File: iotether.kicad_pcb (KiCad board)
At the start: 2 copper layers, 100 x 100 mm, 183 parts, among them J101 USB_B_Micro, J102 Barrel_Jack, J103 Conn_02x04_Odd_Even, J201 Conn_02x04_Top_Bottom, J202 8P8C_LED_Shielded, J203 Conn_01x04, J204 Conn_01x08, J205 Conn_01x04, J206 Conn_01x04, J207 Conn_01x04, J208 Conn_01x04, J301 Conn_01x12, J302 Conn_01x12, J303 Conn_01x12, J304 Conn_01x12, J401 Conn_01x04, J402 Conn_02x04_Odd_Even, J403 Barrel_Jack_Switch, J404 Conn_01x02, J405 Conn_01x02, J406 Conn_01x02, J407 Conn_01x02, J408 Conn_01x04, J409 Conn_01x06, K401 G5LE-1, Q401 DMG3414U, Q402 AO3401A, Q403 AO3401A, Q404 AO3401A, U101 LAN9514, U102 93CxxC, U103 LM1117-3.3, U104 MCP73831-2-OT, U201 SN74CBT3253, U202 PCF8574, U301 FT4232H, U302 93CxxC, U401 MCP2221AxSL, U402 MAX232, U403 PCF8574, U404 PC817, U405 PC817, U406 PC817, U407 PC817, U408 LM75B, U409 DS1307+, Y101 Crystal, Y301 Crystal, Y401 Crystal

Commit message: Add IoTether 2, fix the USB on IoTether 1
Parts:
- J101: footprint Connector_USB:USB_Micro-B_Wuerth_629105150521 -> Connector_PinHeader_2.54mm:PinHeader_1x06_P2.54mm_Vertical
- moved J101 8.54 mm to (77.9, 86.0), turned to 0 degrees
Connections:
- J101 pad 4: Net-(J101-Pad4) -> unconnected-(J101-Pad4)
- J202 pad 4: Net-(J202-Pad4) -> unconnected-(J202-Pad4)
- J202 pad 5: Net-(J202-Pad5) -> unconnected-(J202-Pad5)
- J202 pad 6: Net-(J202-Pad6) -> unconnected-(J202-Pad6)
- J403 pad 3: Net-(J403-Pad3) -> unconnected-(J403-Pad3)
- JP102 pad 2: Net-(JP102-Pad2) -> unconnected-(JP102-Pad2)
- JP103 pad 2: Net-(JP103-Pad2) -> unconnected-(JP103-Pad2)
- JP201 pad 1: Net-(JP201-Pad1) -> unconnected-(JP201-Pad1)
- JP202 pad 1: Net-(JP202-Pad1) -> unconnected-(JP202-Pad1)
- JP203 pad 1: Net-(JP203-Pad1) -> unconnected-(JP203-Pad1)
- JP204 pad 1: Net-(JP204-Pad1) -> unconnected-(JP204-Pad1)
- K401 pad 4: Net-(K401-Pad4) -> unconnected-(K401-Pad4)
- U101 pad 13: Net-(U101-Pad13) -> unconnected-(U101-Pad13)
- U101 pad 31: Net-(U101-Pad31) -> unconnected-(U101-Pad31)
- U101 pad 35: Net-(U101-Pad35) -> unconnected-(U101-Pad35)
- U101 pad 36: Net-(U101-Pad36) -> unconnected-(U101-Pad36)
- U101 pad 37: Net-(U101-Pad37) -> unconnected-(U101-Pad37)
- U101 pad 42: Net-(U101-Pad42) -> unconnected-(U101-Pad42)
- U101 pad 43: Net-(U101-Pad43) -> unconnected-(U101-Pad43)
- U101 pad 45: Net-(U101-Pad45) -> unconnected-(U101-Pad45)
- U101 pad 47: Net-(U101-Pad47) -> unconnected-(U101-Pad47)
- U102 pad 7: Net-(U102-Pad7) -> unconnected-(U102-Pad7)
- U202 pad 13: Net-(U202-Pad13) -> unconnected-(U202-Pad13)
- U301 pad 36: Net-(U301-Pad36) -> unconnected-(U301-Pad36)
- U301 pad 60: Net-(U301-Pad60) -> unconnected-(U301-Pad60)
- U302 pad 7: Net-(U302-Pad7) -> unconnected-(U302-Pad7)
- U401 pad 4: Net-(U401-Pad4) -> unconnected-(U401-Pad4)
- U402 pad 10: Net-(U402-Pad10) -> unconnected-(U402-Pad10)
- U402 pad 7: Net-(U402-Pad7) -> unconnected-(U402-Pad7)
- U402 pad 8: Net-(U402-Pad8) -> unconnected-(U402-Pad8)
- U402 pad 9: Net-(U402-Pad9) -> unconnected-(U402-Pad9)
- U403 pad 13: Net-(U403-Pad13) -> unconnected-(U403-Pad13)
- U408 pad 3: Net-(U408-Pad3) -> unconnected-(U408-Pad3)
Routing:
- net UP_D+: track 32.4 -> 38.5 mm
- net +5V: track 581.3 -> 576.0 mm, vias 17 -> 16
- net UP_D-: track 32.6 -> 37.4 mm
- net GND: track 214.9 -> 212.4 mm
- net VBUS: track 73.2 -> 73.9 mm
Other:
- net class Default removed

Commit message: Add i2c_sampler, update to revision 3
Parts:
- removed C401: 1uF, Capacitor_SMD:C_0805_2012Metric_Pad1.18x1.45mm_HandSolder
- removed C402, C403, C404, C405: 1uF, Capacitor_SMD:C_0805_2012Metric_Pad1.15x1.40mm_HandSolder
- removed D401, D403, D404, D405: LED, LED_SMD:LED_0603_1608Metric_Pad1.05x0.95mm_HandSolder
- removed D402: D, Diode_THT:D_DO-35_SOD27_P2.54mm_Vertical_AnodeUp
- removed J203, J408: Conn_01x04, Connector_PinHeader_2.54mm:PinHeader_1x04_P2.54mm_Vertical
- removed J204: Conn_01x08, Connector_PinHeader_2.54mm:PinHeader_2x04_P2.54mm_Vertical
- removed J401: Conn_01x04, Connector_PinHeader_2.54mm:PinHeader_1x04_P2.54mm_Horizontal
- removed J402: Conn_02x04_Odd_Even, Connector_PinHeader_2.54mm:PinHeader_2x04_P2.54mm_Vertical
- removed J403: Barrel_Jack_Switch, Connector_BarrelJack:BarrelJack_Horizontal
- removed J404, J405, J406, J407: Conn_01x02, TerminalBlock:TerminalBlock_bornier-2_P5.08mm
- removed J409: Conn_01x06, Connector_PinHeader_2.54mm:PinHeader_1x06_P2.54mm_Horizontal
- removed JP401, JP402, JP403: Jumper, Resistor_SMD:R_1206_3216Metric
- removed K401: G5LE-1, Relay_THT:Relay_SPDT_Omron-G5LE-1
- removed Q401: DMG3414U, Package_TO_SOT_SMD:SOT-23
- removed Q402, Q403, Q404: AO3401A, Package_TO_SOT_SMD:SOT-23
- removed R401: 47k, Resistor_SMD:R_0603_1608Metric_Pad1.05x0.95mm_HandSolder
- removed R402, R403: 2.2k, Resistor_SMD:R_0603_1608Metric_Pad1.05x0.95mm_HandSolder
- removed R404, R413, R414, R415: 470, Resistor_SMD:R_0603_1608Metric_Pad1.05x0.95mm_HandSolder
- removed R405, R410, R411, R412: 1k, Resistor_SMD:R_0603_1608Metric_Pad1.05x0.95mm_HandSolder
- removed R406, R407, R408, R409: 100k, Resistor_SMD:R_0603_1608Metric_Pad1.05x0.95mm_HandSolder
- removed RN401: 220, Resistor_THT:R_Array_SIP5
- removed U202, U403: PCF8574, Package_SO:SOIC-16W_7.5x10.3mm_P1.27mm
- removed U401: MCP2221AxSL, Package_SO:SOIC-14_3.9x8.7mm_P1.27mm
- removed U402: MAX232, Package_DIP:DIP-16_W7.62mm_Socket
- removed U404, U405, U406, U407: PC817, Package_DIP:DIP-4_W7.62mm
- added C126: C, Capacitor_SMD:C_0603_1608Metric, B.Cu at (90.9, 97.0)
- added C127: C, Capacitor_THT:CP_Radial_D8.0mm_P3.80mm, F.Cu at (86.3, 93.5)
- added C309: 22pf, Capacitor_SMD:C_0805_2012Metric_Pad1.18x1.45mm_HandSolder, B.Cu at (152.5, 91.5)
- added C310: 22pf, Capacitor_SMD:C_0805_2012Metric_Pad1.18x1.45mm_HandSolder, B.Cu at (152.5, 93.6)
- added C311: C, Capacitor_SMD:C_0603_1608Metric_Pad1.08x0.95mm_HandSolder, F.Cu at (145.1, 138.0)
- added C312: .1uf, Capacitor_SMD:C_0603_1608Metric_Pad1.08x0.95mm_HandSolder, B.Cu at (136.4, 71.3)
- added C313: C, Capacitor_SMD:C_0805_2012Metric_Pad1.18x1.45mm_HandSolder, B.Cu at (140.2, 73.3)
- added C314: C, Capacitor_SMD:C_0805_2012Metric_Pad1.18x1.45mm_HandSolder, B.Cu at (140.2, 70.0)
- added C315: C, Capacitor_SMD:C_0805_2012Metric_Pad1.18x1.45mm_HandSolder, B.Cu at (149.1, 74.5)
- added C316: C, Capacitor_SMD:C_0805_2012Metric_Pad1.18x1.45mm_HandSolder, B.Cu at (147.0, 74.5)
- added D203: LED, LED_SMD:LED_0603_1608Metric_Pad1.05x0.95mm_HandSolder, F.Cu at (125.2, 98.6)
- added J305: Conn_02x04_Odd_Even, Connector_PinHeader_2.54mm:PinHeader_2x04_P2.54mm_Vertical, F.Cu at (122.0, 115.3)
- added J306: Conn_01x09, Connector_USB:USB_A_Wuerth_61400826021_Horizontal_Stacked, F.Cu at (142.9, 59.0)
- added J307: Conn_01x09, Connector_USB:USB_A_Wuerth_61400826021_Horizontal_Stacked, F.Cu at (161.1, 59.0)
- added L102: L, Inductor_SMD:L_1210_3225Metric_Pad1.42x2.65mm_HandSolder, B.Cu at (96.0, 101.6)
- added R107: R, Resistor_SMD:R_0805_2012Metric, B.Cu at (107.7, 98.0)
- added R108: R, Resistor_SMD:R_0603_1608Metric, F.Cu at (92.0, 99.6)
- added R109: R, Resistor_SMD:R_0603_1608Metric, F.Cu at (92.0, 97.9)
- added R224: 470, Resistor_SMD:R_0603_1608Metric_Pad0.98x0.95mm_HandSolder, B.Cu at (128.3, 101.0)
- added R307: R, Resistor_SMD:R_0603_1608Metric_Pad0.98x0.95mm_HandSolder, F.Cu at (147.6, 111.6)
- added R308: R, Resistor_SMD:R_0603_1608Metric_Pad0.98x0.95mm_HandSolder, F.Cu at (147.6, 106.9)
- added R309: R, Resistor_SMD:R_0603_1608Metric_Pad0.98x0.95mm_HandSolder, B.Cu at (112.6, 140.0)
- added R310: R, Resistor_SMD:R_0603_1608Metric_Pad0.98x0.95mm_HandSolder, F.Cu at (149.2, 106.9)
- added R311: R, Resistor_SMD:R_0603_1608Metric_Pad0.98x0.95mm_HandSolder, B.Cu at (113.5, 141.7)
- added R312: 2.2k, Resistor_SMD:R_0603_1608Metric_Pad0.98x0.95mm_HandSolder, B.Cu at (140.9, 111.2)
- added R313: 2.2k, Resistor_SMD:R_0603_1608Metric_Pad0.98x0.95mm_HandSolder, B.Cu at (140.9, 112.8)
- added R314: R, Resistor_SMD:R_0603_1608Metric_Pad0.98x0.95mm_HandSolder, B.Cu at (153.9, 84.9)
- added R315: R, Resistor_SMD:R_0603_1608Metric_Pad0.98x0.95mm_HandSolder, F.Cu at (149.2, 85.6)
- added R316: R, Resistor_SMD:R_0603_1608Metric_Pad0.98x0.95mm_HandSolder, F.Cu at (149.2, 84.0)
- added R317: 15k, Resistor_SMD:R_0603_1608Metric_Pad0.98x0.95mm_HandSolder, B.Cu at (137.4, 67.5)
- added R318: R, Resistor_SMD:R_0603_1608Metric_Pad0.98x0.95mm_HandSolder, B.Cu at (135.7, 65.7)
- added R319: R, Resistor_SMD:R_0603_1608Metric_Pad0.98x0.95mm_HandSolder, B.Cu at (136.2, 60.8)
- added SW301: SW_Push, Button_Switch_THT:SW_PUSH_6mm, F.Cu at (155.8, 116.8)
- added SW302: SW_Push, Button_Switch_THT:SW_PUSH_6mm, F.Cu at (158.8, 96.5)
- added SW303: SW_Push, Button_Switch_THT:SW_PUSH_6mm, F.Cu at (158.8, 82.0)
- added SW304: SW_Push, Button_Switch_THT:SW_PUSH_6mm, F.Cu at (158.8, 72.3)
- added U105: AP62200, Package_TO_SOT_SMD:SOT-23-6, B.Cu at (91.8, 99.7)
- added U303: ATmega328P-P, Package_DIP:DIP-28_W7.62mm, F.Cu at (145.4, 112.8)
- added U304: FE1.1s, Package_SO:SSOP-28_3.9x9.9mm_P0.635mm, F.Cu at (139.4, 64.9)
- added Y302: Crystal, Crystal:Crystal_HC49-U_Vertical, F.Cu at (149.7, 90.0)
- added Y303: Crystal, Crystal:Crystal_HC49-U_Vertical, F.Cu at (149.1, 71.5)
- C102, R101, U409: moved to B.Cu
- C406: footprint Capacitor_SMD:C_0603_1608Metric_Pad1.05x0.95mm_HandSolder -> Capacitor_SMD:C_0603_1608Metric_Pad1.08x0.95mm_HandSolder; moved to F.Cu
- C407: footprint Capacitor_SMD:C_0603_1608Metric_Pad1.05x0.95mm_HandSolder -> Capacitor_SMD:C_0603_1608Metric_Pad1.08x0.95mm_HandSolder
- R106, R210, R211: footprint Resistor_SMD:R_0603_1608Metric_Pad1.05x0.95mm_HandSolder -> Resistor_SMD:R_0603_1608Metric_Pad0.98x0.95mm_HandSolder
- R416: footprint Resistor_SMD:R_0603_1608Metric_Pad1.05x0.95mm_HandSolder -> Resistor_SMD:R_0603_1608Metric_Pad0.98x0.95mm_HandSolder; moved to F.Cu
- moved H105 95.1 mm to (110.7, 135.7)
- moved J103 71.8 mm to (93.1, 79.4), turned to 0 degrees
- moved D406 66.6 mm to (108.5, 115.8), turned to 180 degrees
- moved C406 57.9 mm to (120.7, 118.3), turned to 0 degrees
- moved BT401 56.3 mm to (114.6, 119.4), turned to 90 degrees
- moved R416 55.1 mm to (112.1, 115.8), turned to 0 degrees
- moved Y401 53.8 mm to (118.5, 116.7)
- moved C407 52.9 mm to (118.5, 113.1)
- moved U408 52.1 mm to (107.1, 113.6)
- moved U409 46.2 mm to (112.8, 113.6), turned to 90 degrees
- moved H102 39.9 mm to (163.4, 92.6)
- moved R106 29.9 mm to (141.5, 54.4)
- moved C121 25.6 mm to (159.6, 65.7), turned to 0 degrees
- moved C124 24.8 mm to (129.5, 64.3), turned to -90 degrees
- moved C123 14.1 mm to (143.5, 119.9), turned to 0 degrees
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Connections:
- net /USBHub/SW0 renamed SW0
- net /USBHub/SW1 renamed SW1
- net Net-(J302-Pad3) renamed ATM_RX
- net Net-(J302-Pad4) renamed ATM_TX
- net Net-(J302-Pad7) renamed ATM_DTR
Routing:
- net Net-(R310-Pad2): track 0.00 -> 72.7 mm, vias 0 -> 2
- net Net-(R308-Pad2): track 0.00 -> 72.5 mm, vias 0 -> 2
- net ATM_DTR: track 25.3 -> 67.3 mm, vias 0 -> 1
- net Net-(J409-Pad5): track 40.9 -> 0.00 mm, vias 1 -> 0
- net /MCP2221A/ATM_RESET: track 0.00 -> 38.9 mm, vias 0 -> 3
- net Net-(D402-Pad2): track 33.7 -> 0.00 mm, vias 2 -> 0
- net Net-(RN401-Pad2): track 33.7 -> 0.00 mm
- net Net-(Q401-Pad1): track 32.7 -> 0.00 mm, vias 3 -> 0
- net Net-(J409-Pad4): track 32.6 -> 0.00 mm, vias 1 -> 0
- net Net-(C313-Pad1): track 0.00 -> 32.4 mm, vias 0 -> 4
- net /MCP2221A/232_RX: track 30.6 -> 0.00 mm, vias 3 -> 0
- net EXT_PWR: track 30.5 -> 0.00 mm, vias 2 -> 0
- net /MCP2221A/IN0: track 0.00 -> 29.8 mm, vias 0 -> 1
- net /MCP2221A/232_TX: track 28.9 -> 0.00 mm, vias 2 -> 0
- net Net-(J409-Pad3): track 27.5 -> 0.00 mm, vias 1 -> 0
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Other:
- board size 100 x 100 mm -> 92 x 100 mm
- board text added: "IoTether Rev. 3 2024-01-13 website.peterjin.org/wiki/IoTether"
- board text removed: "Bridge"
- board text removed: "IoTether Rev. 2 2022-01-10 website.peterjin.org/wiki/IoTether"

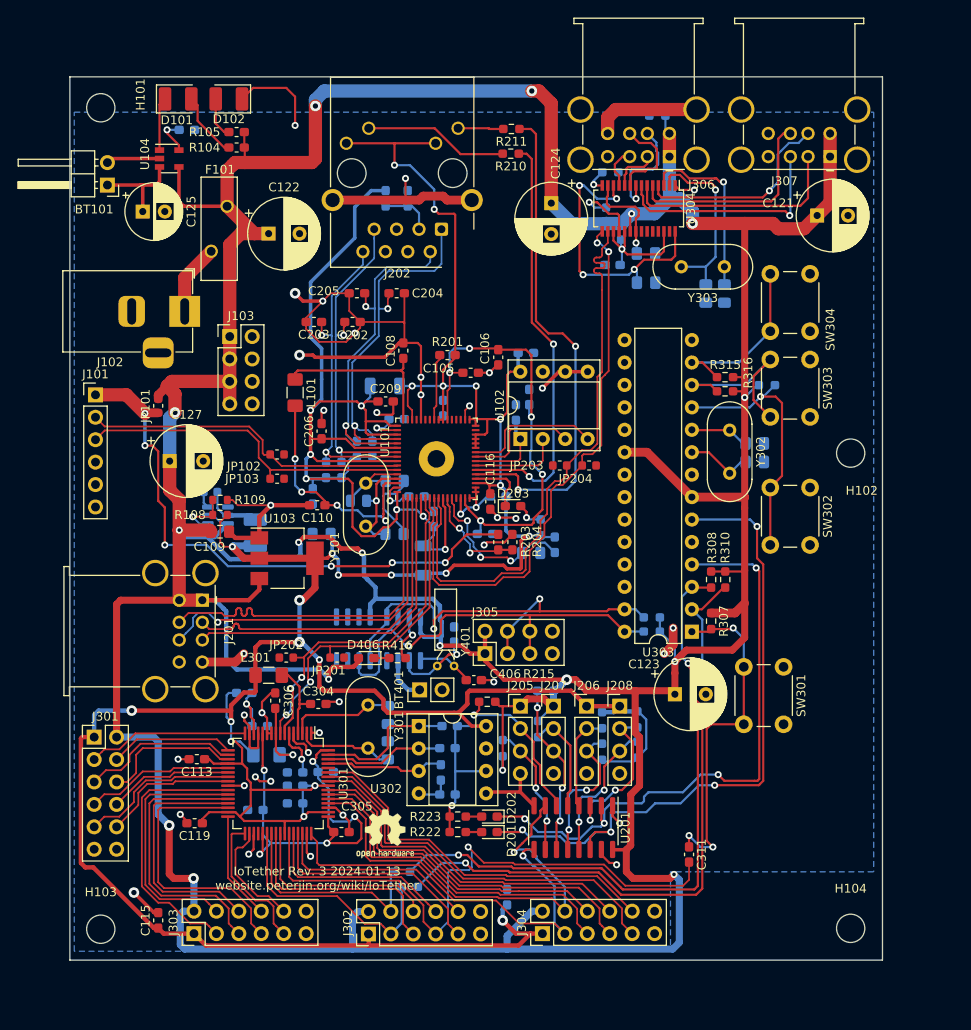
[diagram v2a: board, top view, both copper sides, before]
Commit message: Add 12V->5V regulator
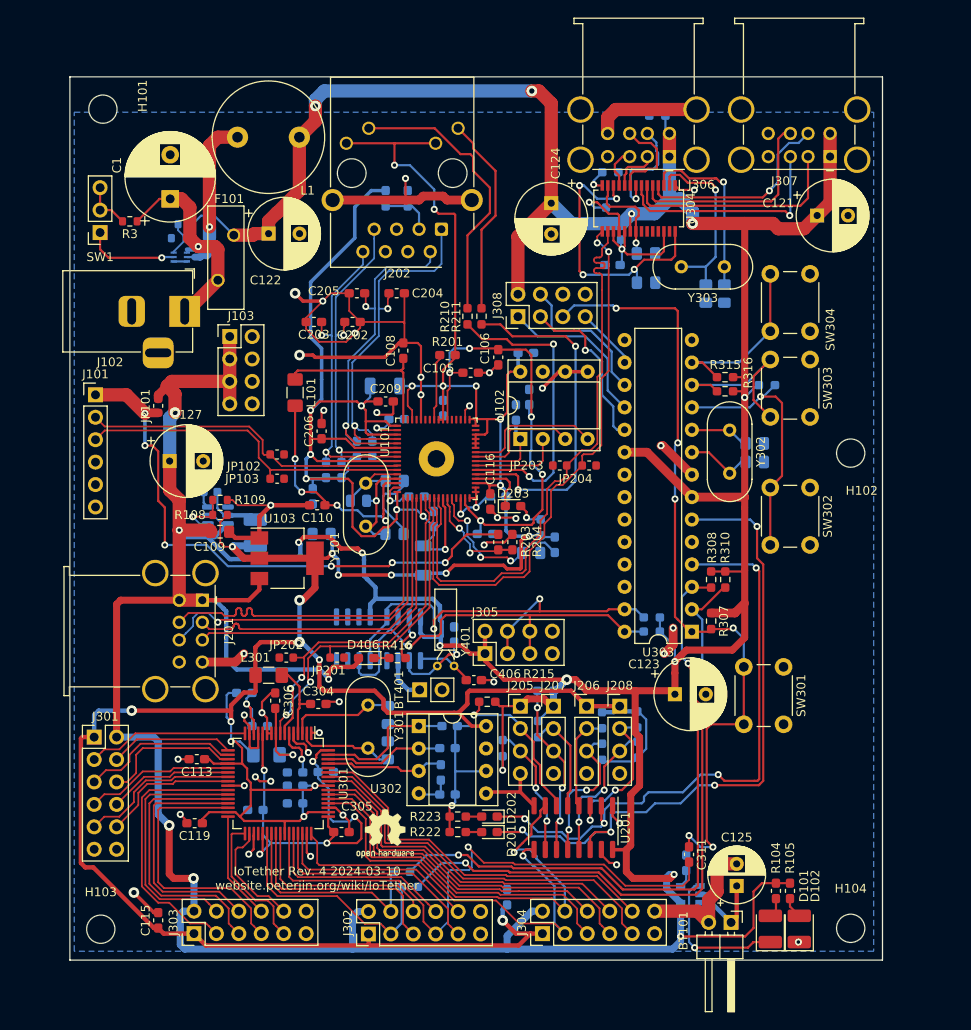
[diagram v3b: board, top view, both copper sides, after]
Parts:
- added C1: C_Polarized, Capacitor_THT:CP_Radial_D10.0mm_P5.00mm, F.Cu at (86.4, 63.8)
- added J1: Conn_02x03_Counter_Clockwise, Package_TO_SOT_SMD:SOT-563, B.Cu at (87.5, 70.4)
- added J308: Conn_02x04_Odd_Even, Connector_PinHeader_2.54mm:PinHeader_2x04_P2.54mm_Vertical, F.Cu at (125.7, 77.2)
- added L1: L, Inductor_THT:L_Radial_D12.5mm_P7.00mm_Fastron_09HCP, F.Cu at (94.0, 56.8)
- added R1: R, Resistor_SMD:R_0603_1608Metric, B.Cu at (88.1, 66.7)
- added R2: R, Resistor_SMD:R_0603_1608Metric, B.Cu at (87.3, 68.3)
- added R3: R, Resistor_SMD:R_0603_1608Metric, F.Cu at (81.8, 66.4)
- added SW1: SW_SPDT, Connector_PinSocket_2.54mm:PinSocket_1x03_P2.54mm_Vertical, F.Cu at (78.4, 67.6)
- U104: moved to B.Cu
- moved D101 115.4 mm to (154.3, 146.5), turned to 90 degrees
- moved D102 114.0 mm to (157.6, 146.5), turned to 90 degrees
- moved BT101 109.3 mm to (149.9, 145.7), turned to -90 degrees
- moved R105 106.3 mm to (156.5, 142.2), turned to -90 degrees
- moved R104 104.0 mm to (154.9, 142.2), turned to -90 degrees
- moved U104 102.1 mm to (145.2, 142.6), turned to 180 degrees
- moved C125 101.7 mm to (150.5, 141.6), turned to 90 degrees
- moved R103 100.4 mm to (144.8, 139.0), turned to -90 degrees
- moved R211 21.5 mm to (121.6, 77.1), turned to 90 degrees
- moved R210 19.1 mm to (120.0, 77.1), turned to 90 degrees
- moved F101 3.36 mm to (93.6, 67.9)
- moved H101 0.29 mm to (78.7, 53.7)
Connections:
- U303 pad 16: unconnected-(U303-Pad16) -> /MCP2221A/ISP_SS
- U303 pad 17: unconnected-(U303-Pad17) -> /MCP2221A/ISP_MOSI
- U303 pad 18: unconnected-(U303-Pad18) -> /MCP2221A/ISP_MISO
- U303 pad 19: unconnected-(U303-Pad19) -> /MCP2221A/ISP_SCK
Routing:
- net /MCP2221A/ATM_RESET: track 38.9 -> 90.0 mm, vias 3 -> 6
- net /MCP2221A/ISP_SCK: track 0.00 -> 19.3 mm, vias 0 -> 1
- net /MCP2221A/ISP_MISO: track 0.00 -> 18.4 mm
- net Net-(J1-Pad2): track 0.00 -> 18.4 mm, vias 0 -> 1
- net Net-(J202-Pad9): track 5.16 -> 22.8 mm
- net LNKA_LED: track 57.5 -> 40.3 mm
- net Net-(C1-Pad1): track 8.04 -> 25.1 mm, vias 0 -> 1
- net /MCP2221A/ISP_MOSI: track 0.00 -> 16.6 mm
- net Net-(J202-Pad11): track 16.4 -> 32.1 mm
- net SPD_LED: track 48.0 -> 35.0 mm
- net Net-(D101-Pad1): track 6.06 -> 17.0 mm, vias 0 -> 1
- net Net-(J1-Pad5): track 0.00 -> 10.7 mm, vias 0 -> 1
- net GND: track 215.8 -> 223.0 mm, vias 38 -> 39
- net /MCP2221A/ISP_SS: track 0.00 -> 7.03 mm
- net Net-(R3-Pad2): track 0.00 -> 5.61 mm
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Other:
- board text added: "IoTether Rev. 4 2024-03-10 website.peterjin.org/wiki/IoTether"
- board text removed: "IoTether Rev. 3 2024-01-13 website.peterjin.org/wiki/IoTether"
